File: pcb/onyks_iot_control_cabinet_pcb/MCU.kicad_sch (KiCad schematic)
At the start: 14 parts, among them J10 Conn_01x06_Pin, J9 Conn_02x05_Odd_Even, Q1 NPN, Q2 NPN, SW2 SW_Push, SW3 SW_Push, U1 ESP32-WROOM-32D

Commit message: New fixes of schematics
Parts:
- C1, C11, C2: value 0.1u -> 0.1u/50V; footprint Capacitor_SMD:C_0805_2012Metric -> Capacitor_SMD:C_0603_1608Metric
- C10: value 22u -> 22u/10V; footprint Capacitor_SMD:C_0805_2012Metric -> Capacitor_SMD:C_0603_1608Metric
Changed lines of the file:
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@@
 			)
 		)
-		(property "Value" "0.1u"
-			(at 133.096 45.974 90)
+		(property "Value" "0.1u/50V"
+			(at 135.128 45.974 90)
 			(effects
 				(font
@@
 			)
 		)
-		(property "Footprint" "Capacitor_SMD:C_0805_2012Metric"
+		(property "Footprint" "Capacitor_SMD:C_0603_1608Metric"
 			(at 134.62 48.5648 0)
 			(effects
@@
 			)
 		)
-		(property "Value" "0.1u"
-			(at 34.798 118.872 0)
-			(effects
-				(font
-					(size 1.27 1.27)
-				)
-			)
-		)
-		(property "Footprint" "Capacitor_SMD:C_0805_2012Metric"
+		(property "Value" "0.1u/50V"
+			(at 32.258 119.126 0)
+			(effects
+				(font
+					(size 1.27 1.27)
+				)
+			)
+		)
+		(property "Footprint" "Capacitor_SMD:C_0603_1608Metric"
 			(at 39.0652 119.38 0)
 			(effects
@@
 			)
 		)
-		(property "Value" "0.1u"
-			(at 54.102 119.126 0)
-			(effects
-				(font
-					(size 1.27 1.27)
-				)
-			)
-		)
-		(property "Footprint" "Capacitor_SMD:C_0805_2012Metric"
+		(property "Value" "0.1u/50V"
+			(at 51.816 112.776 0)
+			(effects
+				(font
+					(size 1.27 1.27)
+				)
+			)
+		)
+		(property "Footprint" "Capacitor_SMD:C_0603_1608Metric"
 			(at 58.1152 119.38 0)
 			(effects
@@
 			)
 		)
-		(property "Value" "22u"
-			(at 132.842 57.404 90)
+		(property "Value" "22u/10V"
+			(at 134.112 57.404 90)
 			(effects
 				(font
@@
 			)
 		)
-		(property "Footprint" "Capacitor_SMD:C_0805_2012Metric"
+		(property "Footprint" "Capacitor_SMD:C_0603_1608Metric"
 			(at 134.62 59.9948 0)
 			(effects

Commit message: Quick Fixes
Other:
- note added: "DIODA RGB"
- moved on the sheet: D1, Q1, Q2, R1, R2

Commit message: PCB Review 2.0 Update
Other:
- moved on the sheet: C10, C11

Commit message: Quick fixes
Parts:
- renumbered C10 to C3, C11 to C4, J9 to J1, J10 to J2, SW2 to SW1, SW3 to SW2
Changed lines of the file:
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@@
 		(on_board yes)
 		(dnp no)
-		(property "Reference" "C11"
+		(property "Reference" "C4"
 			(at 132.588 54.102 90)
 			(effects
@@
 			(project "onyks_iot_control_cabinet_pcb"
 				(path "/789878cb-67d5-4bc7-a42d-b3bc72d661d0/13ebc194-338a-49a6-8327-5cf2c633b763"
-					(reference "C11")
+					(reference "C4")
 					(unit 1)
 				)
@@
 		(dnp no)
 		(fields_autoplaced yes)
-		(property "Reference" "#PWR04"
+		(property "Reference" "#PWR08"
 			(at 38.1 72.39 0)
 			(effects
@@
 			(project "onyks_iot_control_cabinet_pcb"
 				(path "/789878cb-67d5-4bc7-a42d-b3bc72d661d0/13ebc194-338a-49a6-8327-5cf2c633b763"
-					(reference "#PWR04")
+					(reference "#PWR08")
 					(unit 1)
 				)
@@
 		(on_board yes)
 		(dnp no)
-		(property "Reference" "#PWR02"
+		(property "Reference" "#PWR09"
 			(at 49.53 127 0)
 			(effects
@@
 			(project "onyks_iot_control_cabinet_pcb"
 				(path "/789878cb-67d5-4bc7-a42d-b3bc72d661d0/13ebc194-338a-49a6-8327-5cf2c633b763"
-					(reference "#PWR02")
+					(reference "#PWR09")
 					(unit 1)
 				)
@@
 		(dnp no)
 		(fields_autoplaced yes)
-		(property "Reference" "#PWR03"
+		(property "Reference" "#PWR06"
 			(at 39.37 52.07 0)
 			(effects
@@
 			(project "onyks_iot_control_cabinet_pcb"
 				(path "/789878cb-67d5-4bc7-a42d-b3bc72d661d0/13ebc194-338a-49a6-8327-5cf2c633b763"
-					(reference "#PWR03")
+					(reference "#PWR06")
 					(unit 1)
 				)
@@
 		(on_board yes)
 		(dnp no)
-		(property "Reference" "#PWR01"
+		(property "Reference" "#PWR05"
 			(at 39.37 39.37 0)
 			(effects
@@
 			(project "onyks_iot_control_cabinet_pcb"
 				(path "/789878cb-67d5-4bc7-a42d-b3bc72d661d0/13ebc194-338a-49a6-8327-5cf2c633b763"
-					(reference "#PWR01")
+					(reference "#PWR05")
 					(unit 1)
 				)
@@
 		(on_board yes)
 		(dnp no)
-		(property "Reference" "#PWR039"
+		(property "Reference" "#PWR013"
 			(at 189.23 121.92 0)
 			(effects
@@
 			(project "onyks_iot_control_cabinet_pcb"
 				(path "/789878cb-67d5-4bc7-a42d-b3bc72d661d0/13ebc194-338a-49a6-8327-5cf2c633b763"
-					(reference "#PWR039")
+					(reference "#PWR013")
 					(unit 1)
 				)
@@
 		(dnp no)
 		(fields_autoplaced yes)
-		(property "Reference" "#PWR08"
+		(property "Reference" "#PWR010"
 			(at 123.19 50.8 0)
 			(effects
@@
 			(project "onyks_iot_control_cabinet_pcb"
 				(path "/789878cb-67d5-4bc7-a42d-b3bc72d661d0/13ebc194-338a-49a6-8327-5cf2c633b763"
-					(reference "#PWR08")
+					(reference "#PWR010")
 					(unit 1)
 				)
@@
 		(on_board yes)
 		(dnp no)
-		(property "Reference" "#PWR040"
+		(property "Reference" "#PWR014"
 			(at 189.23 143.51 0)
 			(effects
@@
 			(project "onyks_iot_control_cabinet_pcb"
 				(path "/789878cb-67d5-4bc7-a42d-b3bc72d661d0/13ebc194-338a-49a6-8327-5cf2c633b763"
-					(reference "#PWR040")
+					(reference "#PWR014")
 					(unit 1)
 				)
@@
 		(on_board yes)
 		(dnp no)
-		(property "Reference" "#PWR036"
+		(property "Reference" "#PWR011"
 			(at 123.19 149.86 0)
 			(effects
@@
 			(project "onyks_iot_control_cabinet_pcb"
 				(path "/789878cb-67d5-4bc7-a42d-b3bc72d661d0/13ebc194-338a-49a6-8327-5cf2c633b763"
-					(reference "#PWR036")
+					(reference "#PWR011")
 					(unit 1)
 				)
@@
 		(on_board yes)
 		(dnp no)
-		(property "Reference" "SW2"
+		(property "Reference" "SW1"
 			(at 47.244 118.618 90)
 			(effects
@@
 			(project "onyks_iot_control_cabinet_pcb"
 				(path "/789878cb-67d5-4bc7-a42d-b3bc72d661d0/13ebc194-338a-49a6-8327-5cf2c633b763"
-					(reference "SW2")
+					(reference "SW1")
 					(unit 1)
 				)
@@
 		(on_board yes)
 		(dnp no)
-		(property "Reference" "#PWR037"
+		(property "Reference" "#PWR012"
 			(at 138.43 69.85 0)
 			(effects
@@
 			(project "onyks_iot_control_cabinet_pcb"
 				(path "/789878cb-67d5-4bc7-a42d-b3bc72d661d0/13ebc194-338a-49a6-8327-5cf2c633b763"
-					(reference "#PWR037")
+					(reference "#PWR012")
 					(unit 1)
 				)
@@
 		(dnp no)
 		(fields_autoplaced yes)
-		(property "Reference" "J10"
+		(property "Reference" "J2"
 			(at 58.42 74.9299 0)
 			(effects
@@
 			(project "onyks_iot_control_cabinet_pcb"
 				(path "/789878cb-67d5-4bc7-a42d-b3bc72d661d0/13ebc194-338a-49a6-8327-5cf2c633b763"
-					(reference "J10")
+					(reference "J2")
 					(unit 1)
 				)
@@
 		(on_board yes)
 		(dnp no)
-		(property "Reference" "J9"
+		(property "Reference" "J1"
 			(at 50.8 32.766 0)
 			(effects
@@
 			(project "onyks_iot_control_cabinet_pcb"
 				(path "/789878cb-67d5-4bc7-a42d-b3bc72d661d0/13ebc194-338a-49a6-8327-5cf2c633b763"
-					(reference "J9")
+					(reference "J1")
 					(unit 1)
 				)
@@
 		(on_board yes)
 		(dnp no)
-		(property "Reference" "#PWR05"
+		(property "Reference" "#PWR07"
 			(at 43.18 73.66 0)
 			(effects
@@
 			(project "onyks_iot_control_cabinet_pcb"
 				(path "/789878cb-67d5-4bc7-a42d-b3bc72d661d0/13ebc194-338a-49a6-8327-5cf2c633b763"
-					(reference "#PWR05")
+					(reference "#PWR07")
 					(unit 1)
 				)
@@
 		(on_board yes)
 		(dnp no)
-		(property "Reference" "SW3"
+		(property "Reference" "SW2"
 			(at 66.294 118.618 90)
 			(effects
@@
 			(project "onyks_iot_control_cabinet_pcb"
 				(path "/789878cb-67d5-4bc7-a42d-b3bc72d661d0/13ebc194-338a-49a6-8327-5cf2c633b763"
-					(reference "SW3")
+					(reference "SW2")
 					(unit 1)
 				)
@@
 		(on_board yes)
 		(dnp no)
-		(property "Reference" "C10"
+		(property "Reference" "C3"
 			(at 132.588 43.942 90)
 			(effects
@@
 			(project "onyks_iot_control_cabinet_pcb"
 				(path "/789878cb-67d5-4bc7-a42d-b3bc72d661d0/13ebc194-338a-49a6-8327-5cf2c633b763"
-					(reference "C10")
-					(unit 1)
-				)
+					(reference "C3")
+					(unit 1)
+				)

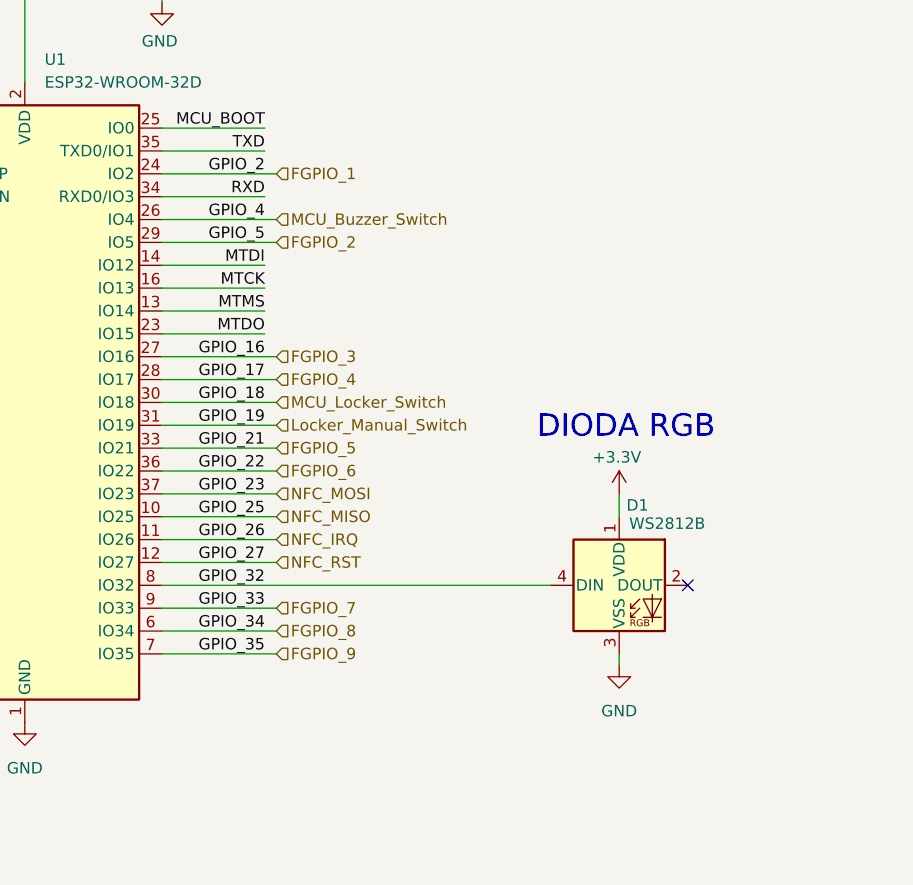
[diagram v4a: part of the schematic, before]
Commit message: Update of the power supply and added the header for 125kHz RFID
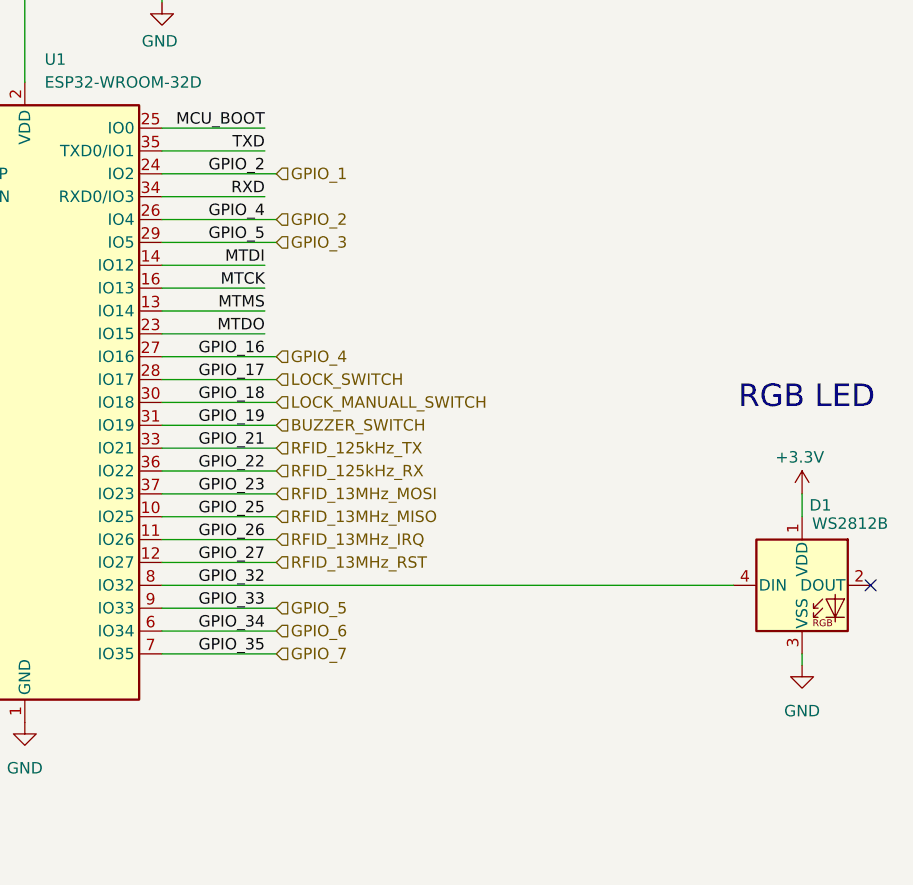
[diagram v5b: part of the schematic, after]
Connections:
- net FGPIO_3 is gone; now on net GPIO_1: U1.27 (IO16)
- net FGPIO_7 is gone; now on net GPIO_3: U1.9 (IO33)
- net MCU_Buzzer_Switch is gone; now on net GPIO_1: U1.26 (IO4)
- net FGPIO_1 renamed GPIO_1
- net FGPIO_2 renamed GPIO_3
- net FGPIO_4 renamed LOCK_SWITCH
- net FGPIO_5 renamed RFID_125kHz_TX
- net FGPIO_6 renamed RFID_125kHz_RX
- net FGPIO_8 renamed GPIO_6
- net FGPIO_9 renamed GPIO_7
- net Locker_Manual_Switch renamed BUZZER_SWITCH
- net MCU_Locker_Switch renamed LOCK_MANUALL_SWITCH
- net NFC_IRQ renamed RFID_13MHz_IRQ
- net NFC_MISO renamed RFID_13MHz_MISO
- net NFC_MOSI renamed RFID_13MHz_MOSI
- net NFC_RST renamed RFID_13MHz_RST
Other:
- note added: "RGB LED"
- note removed: "DIODA RGB"
- company: (none) -> ,,Onyks'' Students Scientific Association
- title: (none) -> Onyks Iot Control Cabinet
- moved on the sheet: D1
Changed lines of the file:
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@@
 	(generator_version "9.0")
 	(paper "A4")
+	(title_block
+		(title "Onyks Iot Control Cabinet")
+		(date "2025-08-25")
+		(rev "v1.0")
+		(company ",,Onyks'' Students Scientific Association")
+		(comment 1 "Karol Ambroziński")
+		(comment 2 "Jakub Jastrzębski")
+	)
 	(text "ESP32 UART"
 		(exclude_from_sim no)
@@
 		)
 	)
-	(text "DIODA RGB\n"
+	(text "RGB LED"
 		(exclude_from_sim no)
-		(at 189.992 110.744 0)
+		(at 210.058 107.442 0)
 		(effects
 			(font
@@
 	)
 	(no_connect
-		(at 196.85 128.27)
+		(at 217.17 128.27)
 	)
 	(no_connect
@@
 	(wire
 		(pts
-			(xy 138.43 128.27) (xy 181.61 128.27)
+			(xy 138.43 128.27) (xy 201.93 128.27)
 		)
 		(stroke
@@
 	(wire
 		(pts
-			(xy 189.23 118.11) (xy 189.23 120.65)
+			(xy 209.55 118.11) (xy 209.55 120.65)
 		)
 		(stroke
@@
 	(wire
 		(pts
-			(xy 189.23 135.89) (xy 189.23 137.16)
+			(xy 209.55 135.89) (xy 209.55 137.16)
 		)
 		(stroke
@@
 		)
 	)
-	(hierarchical_label "FGPIO_3"
+	(hierarchical_label "RFID_13MHz_RST"
+		(shape input)
+		(at 151.13 125.73 0)
+		(effects
+			(font
+				(size 1.27 1.27)
+			)
+			(justify left)
+		)
+	)
+	(hierarchical_label "GPIO_4"
 		(shape input)
 		(at 151.13 102.87 0)
@@
 		)
 	)
-	(hierarchical_label "FGPIO_8"
+	(hierarchical_label "LOCK_MANUALL_SWITCH"
+		(shape input)
+		(at 151.13 107.95 0)
+		(effects
+			(font
+				(size 1.27 1.27)
+			)
+			(justify left)
+		)
+	)
+	(hierarchical_label "GPIO_6"
 		(shape input)
 		(at 151.13 133.35 0)
@@
 		)
 	)
-	(hierarchical_label "MCU_Locker_Switch"
+	(hierarchical_label "GPIO_2"
 		(shape input)
-		(at 151.13 107.95 0)
+		(at 151.13 87.63 0)
 		(effects
 			(font
@@
 		)
 	)
-	(hierarchical_label "NFC_MOSI"
+	(hierarchical_label "RFID_125kHz_RX"
+		(shape input)
+		(at 151.13 115.57 0)
+		(effects
+			(font
+				(size 1.27 1.27)
+			)
+			(justify left)
+		)
+	)
+	(hierarchical_label "RFID_13MHz_MISO"
+		(shape input)
+		(at 151.13 120.65 0)
+		(effects
+			(font
+				(size 1.27 1.27)
+			)
+			(justify left)
+		)
+	)
+	(hierarchical_label "RFID_13MHz_IRQ"
+		(shape input)
+		(at 151.13 123.19 0)
+		(effects
+			(font
+				(size 1.27 1.27)
+			)
+			(justify left)
+		)
+	)
+	(hierarchical_label "BUZZER_SWITCH"
+		(shape input)
+		(at 151.13 110.49 0)
+		(effects
+			(font
+				(size 1.27 1.27)
+			)
+			(justify left)
+		)
+	)
+	(hierarchical_label "RFID_125kHz_TX"
+		(shape input)
+		(at 151.13 113.03 0)
+		(effects
+			(font
+				(size 1.27 1.27)
+			)
+			(justify left)
+		)
+	)
+	(hierarchical_label "GPIO_5"
+		(shape input)
+		(at 151.13 130.81 0)
+		(effects
+			(font
+				(size 1.27 1.27)
+			)
+			(justify left)
+		)
+	)
+	(hierarchical_label "RFID_13MHz_MOSI"
 		(shape input)
 		(at 151.13 118.11 0)
@@
 		)
 	)
-	(hierarchical_label "Locker_Manual_Switch"
-		(shape input)
-		(at 151.13 110.49 0)
-		(effects
-			(font
-				(size 1.27 1.27)
-			)
-			(justify left)
-		)
-	)
-	(hierarchical_label "NFC_MISO"
-		(shape input)
-		(at 151.13 120.65 0)
-		(effects
-			(font
-				(size 1.27 1.27)
-			)
-			(justify left)
-		)
-	)
-	(hierarchical_label "NFC_IRQ"
-		(shape input)
-		(at 151.13 123.19 0)
-		(effects
-			(font
-				(size 1.27 1.27)
-			)
-			(justify left)
-		)
-	)
-	(hierarchical_label "FGPIO_6"
-		(shape input)
-		(at 151.13 115.57 0)
-		(effects
-			(font
-				(size 1.27 1.27)
-			)
-			(justify left)
-		)
-	)
-	(hierarchical_label "FGPIO_7"
-		(shape input)
-		(at 151.13 130.81 0)
-		(effects
-			(font
-				(size 1.27 1.27)
-			)
-			(justify left)
-		)
-	)
-	(hierarchical_label "NFC_RST"
-		(shape input)
-		(at 151.13 125.73 0)
-		(effects
-			(font
-				(size 1.27 1.27)
-			)
-			(justify left)
-		)
-	)
-	(hierarchical_label "MCU_Buzzer_Switch"
-		(shape input)
-		(at 151.13 87.63 0)
-		(effects
-			(font
-				(size 1.27 1.27)
-			)
-			(justify left)
-		)
-	)
-	(hierarchical_label "FGPIO_2"
+	(hierarchical_label "GPIO_3"
 		(shape input)
 		(at 151.13 90.17 0)
@@
 		)
 	)
-	(hierarchical_label "FGPIO_5"
+	(hierarchical_label "LOCK_SWITCH"
 		(shape input)
-		(at 151.13 113.03 0)
+		(at 151.13 105.41 0)
 		(effects
 			(font
@@
 		)
 	)
-	(hierarchical_label "FGPIO_1"
+	(hierarchical_label "GPIO_1"
 		(shape input)
 		(at 151.13 82.55 0)
@@
 		)
 	)
-	(hierarchical_label "FGPIO_9"
+	(hierarchical_label "GPIO_7"
 		(shape input)
 		(at 151.13 135.89 0)
-		(effects
-			(font
-				(size 1.27 1.27)
-			)
-			(justify left)
-		)
-	)
-	(hierarchical_label "FGPIO_4"
-		(shape input)
-		(at 151.13 105.41 0)
 		(effects
 			(font
@@
 	(symbol
 		(lib_id "power:+3.3V")
-		(at 189.23 118.11 0)
+		(at 209.55 118.11 0)
 		(unit 1)
 		(exclude_from_sim no)
@@
 		(dnp no)
 		(property "Reference" "#PWR013"
-			(at 189.23 121.92 0)
+			(at 209.55 121.92 0)
 			(effects
 				(font
@@
 		)
 		(property "Value" "+3.3V"
-			(at 188.976 114.046 0)
+			(at 209.296 114.046 0)
 			(effects
 				(font
@@
 		)
 		(property "Footprint" ""
-			(at 189.23 118.11 0)
+			(at 209.55 118.11 0)
 			(effects
 				(font
@@
 		)
 		(property "Datasheet" ""
-			(at 189.23 118.11 0)
+			(at 209.55 118.11 0)
 			(effects
 				(font
@@
 		)
 		(property "Description" ""
-			(at 189.23 118.11 0)
+			(at 209.55 118.11 0)
 			(effects
 				(font
@@
 	(symbol
 		(lib_id "LED:WS2812B")
-		(at 189.23 128.27 0)
+		(at 209.55 128.27 0)
 		(unit 1)
 		(exclude_from_sim no)
@@
 		(dnp no)
 		(property "Reference" "D1"
-			(at 191.262 119.38 0)
+			(at 211.582 119.38 0)
 			(effects
 				(font
@@
 		)
 		(property "Value" "WS2812B"
-			(at 194.564 121.412 0)
+			(at 214.884 121.412 0)
 			(effects
 				(font
@@
 		)
 		(property "Footprint" "LED_SMD:LED_WS2812B_PLCC4_5.0x5.0mm_P3.2mm"
-			(at 190.5 135.89 0)
+			(at 210.82 135.89 0)
 			(effects
 				(font
@@
 		)
 		(property "Datasheet" "https://cdn-shop.adafruit.com/datasheets/WS2812B.pdf"
-			(at 191.77 137.795 0)
+			(at 212.09 137.795 0)
 			(effects
 				(font
@@
 		)
 		(property "Description" "RGB LED with integrated controller"
-			(at 189.23 128.27 0)
+			(at 209.55 128.27 0)
 			(effects
 				(font
@@
 	(symbol
 		(lib_id "power:GND")
-		(at 189.23 137.16 0)
+		(at 209.55 137.16 0)
 		(unit 1)
 		(exclude_from_sim no)
@@
 		(dnp no)
 		(property "Reference" "#PWR014"
-			(at 189.23 143.51 0)
+			(at 209.55 143.51 0)
 			(effects
 				(font
@@
 		)
 		(property "Value" "GND"
-			(at 189.23 142.24 0)
+			(at 209.55 142.24 0)
 			(effects
 				(font
@@
 		)
 		(property "Footprint" ""
-			(at 189.23 137.16 0)
+			(at 209.55 137.16 0)
 			(effects
 				(font
@@
 		)
 		(property "Datasheet" ""
-			(at 189.23 137.16 0)
+			(at 209.55 137.16 0)
 			(effects
 				(font
@@
 		)
 		(property "Description" ""
-			(at 189.23 137.16 0)
-			(effects
-				(font
+			(at 209.55 137.16 0)
+			(effects
+				(font

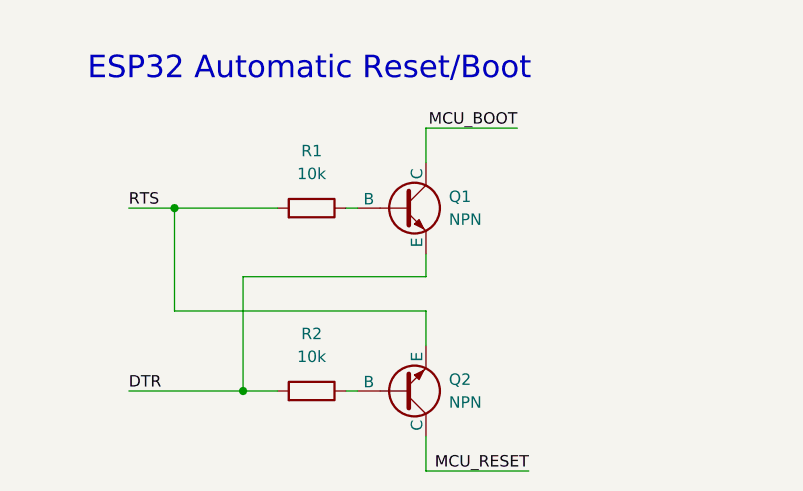
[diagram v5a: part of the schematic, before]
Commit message: Schematics update; power supply and footprints fixes
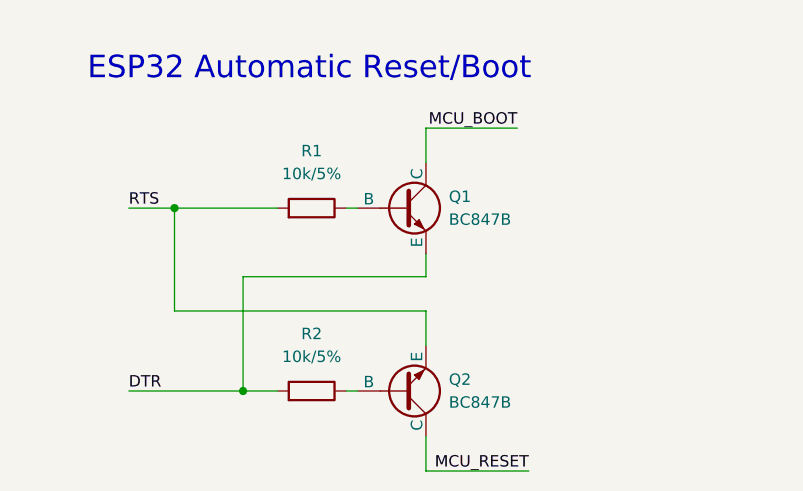
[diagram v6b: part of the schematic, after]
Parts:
- Q1, Q2: value NPN -> BC847B
- R1, R2: value 10k -> 10k/5%
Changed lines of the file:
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@@
 			)
 		)
-		(property "Value" "10k"
+		(property "Value" "10k/5%"
 			(at 52.07 153.67 90)
 			(effects
@@
 			)
 		)
-		(property "Value" "NPN"
+		(property "Value" "BC847B"
 			(at 67.31 158.7499 0)
 			(effects
@@
 			)
 		)
-		(property "Value" "NPN"
+		(property "Value" "BC847B"
 			(at 67.31 179.0699 0)
 			(effects
@@
 			)
 		)
-		(property "Value" "10k"
+		(property "Value" "10k/5%"
 			(at 52.07 173.99 90)
 			(effects
